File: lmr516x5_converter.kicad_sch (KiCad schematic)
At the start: 8 parts, among them U1 LMR516x5

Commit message: sch: first draft
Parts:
- added C1: 10uF 100V, Capacitor_SMD:C_1210_3225Metric, symbol Device:C_Small
- added C3: 0.1uF, Capacitor_SMD:C_0603_1608Metric, symbol Device:C_Small
- C1, C4: value 22uF 16V -> 10uF 50V
- R1: value 52.3k -> Vchoice; footprint Resistor_SMD:R_0603_1608Metric -> SMD:0603_1608Metric_DNI_NoPaste
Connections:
- net GND: now also C1.2, C3.2
- net Vin: now also C1.1, C3.1
- net 5V renamed Vout
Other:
- note added: "Just one of these entry capacitors seem be enough according to the datasheet."
- note added: "Vin max = 60V Vout max = 30V"
- moved on the sheet: C1, C2, C3, C4, L1, R1, R2, U1

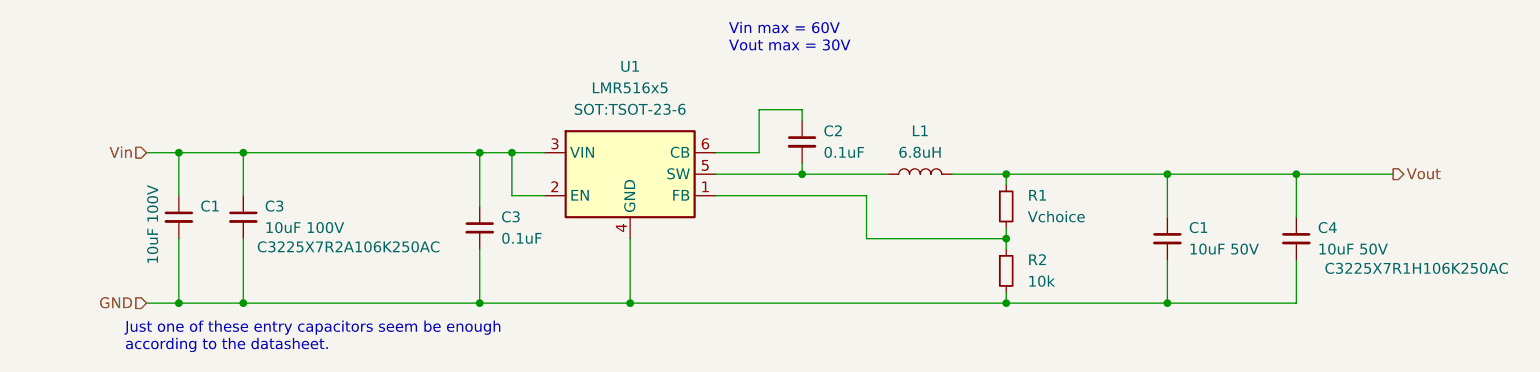
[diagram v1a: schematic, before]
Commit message: Change entry 0.1uF cap to 1uF 100V
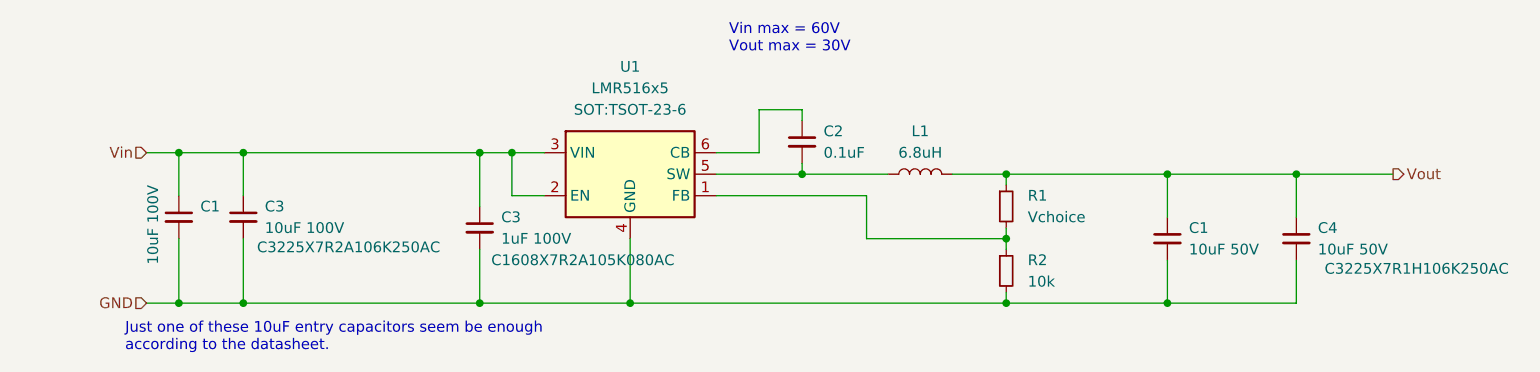
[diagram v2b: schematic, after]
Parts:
- C3: value 0.1uF -> 1uF 100V
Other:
- note added: "Just one of these 10uF entry capacitors seem be enough according to the datasheet."
- note removed: "Just one of these entry capacitors seem be enough according to the datasheet."
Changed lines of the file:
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@@
 		)
 	)
-	(text "Just one of these entry capacitors seem be enough\naccording to the datasheet."
+	(text "Just one of these 10uF entry capacitors seem be enough\naccording to the datasheet."
 		(exclude_from_sim no)
 		(at 36.83 53.594 0)
@@
 		(on_board yes)
 		(dnp no)
-		(fields_autoplaced yes)
 		(property "Reference" "C3"
 			(at 81.28 39.3762 0)
@@
 			)
 		)
-		(property "Value" "0.1uF"
+		(property "Value" "1uF 100V"
 			(at 81.28 41.9162 0)
 			(effects
@@
 			)
 		)
-		(property "Description" "Unpolarized capacitor, small symbol"
-			(at 78.74 40.64 0)
-			(effects
-				(font
-					(size 1.27 1.27)
-				)
-				(hide yes)
-			)
-		)
+		(property "Description" "C1608X7R2A105K080AC"
+			(at 90.932 44.45 0)
+			(effects
+				(font
+					(size 1.27 1.27)
+				)
+			)
+		)

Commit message: First placement
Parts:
- added C7: Csnub, Capacitor_SMD:C_0402_1005Metric, symbol Device:C_Small
- added R4: Rsnub, Resistor_SMD:R_0402_1005Metric, symbol Device:R_Small
- C1, C3: footprint Capacitor_SMD:C_1210_3225Metric -> SMD:C_1210_3225Metric_Tight
- C2, C3: footprint Capacitor_SMD:C_0603_1608Metric -> SMD:C_0603_1608Metric_Tight
- R1: footprint SMD:0603_1608Metric_DNI_NoPaste -> Resistor_SMD:R_0603_1608Metric
- U1: footprint SOT:TSOT-23-6 -> SOT:TSOT-23-6_Tight
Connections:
- net GND: now also R4.2
- net FB: now reaches R1.2, R2.1, U1.1 (FB)
- net at C2.2, L1.1, U1.5 (SW): now also C7.1
- new net: C7.2, R4.1
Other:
- note removed: "Just one of these 10uF entry capacitors seem be enough according to the datasheet."
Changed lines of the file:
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@@
 	(paper "A4")
 	(junction
+		(at 140.97 41.91)
+		(diameter 0)
+		(color 0 0 0 0)
+	)
+	(junction
+		(at 116.84 49.53)
+		(diameter 0)
+		(color 0 0 0 0)
+	)
+	(junction
 		(at 140.97 34.29)
 		(diameter 0)
@@
 	)
 	(junction
-		(at 140.97 41.91)
-		(diameter 0)
-		(color 0 0 0 0)
-	)
-	(junction
 		(at 116.84 34.29)
 		(diameter 0)
@@
 	(wire
 		(pts
+			(xy 116.84 34.29) (xy 116.84 36.83)
+		)
+		(stroke
+			(width 0)
+			(type default)
+		)
+	)
+	(wire
+		(pts
 			(xy 50.8 31.75) (xy 78.74 31.75)
 		)
@@
 	(wire
 		(pts
+			(xy 116.84 49.53) (xy 140.97 49.53)
+		)
+		(stroke
+			(width 0)
+			(type default)
+		)
+	)
+	(wire
+		(pts
 			(xy 50.8 49.53) (xy 78.74 49.53)
 		)
@@
 	(wire
 		(pts
-			(xy 96.52 49.53) (xy 140.97 49.53)
+			(xy 96.52 49.53) (xy 116.84 49.53)
 		)
 		(stroke
@@
 	(wire
 		(pts
+			(xy 140.97 41.91) (xy 140.97 43.18)
+		)
+		(stroke
+			(width 0)
+			(type default)
+		)
+	)
+	(wire
+		(pts
 			(xy 96.52 49.53) (xy 96.52 41.91)
 		)
@@
 	(wire
 		(pts
-			(xy 124.46 36.83) (xy 124.46 41.91)
-		)
-		(stroke
-			(width 0)
-			(type default)
-		)
-	)
-	(wire
-		(pts
-			(xy 124.46 41.91) (xy 140.97 41.91)
+			(xy 116.84 48.26) (xy 116.84 49.53)
 		)
 		(stroke
@@
 	(wire
 		(pts
+			(xy 106.68 36.83) (xy 110.49 36.83)
+		)
+		(stroke
+			(width 0)
+			(type default)
+		)
+	)
+	(wire
+		(pts
 			(xy 140.97 49.53) (xy 160.02 49.53)
 		)
@@
 	(wire
 		(pts
-			(xy 106.68 36.83) (xy 124.46 36.83)
-		)
-		(stroke
-			(width 0)
-			(type default)
-		)
-	)
-	(wire
-		(pts
 			(xy 78.74 31.75) (xy 82.55 31.75)
 		)
@@
 	(wire
 		(pts
-			(xy 140.97 41.91) (xy 140.97 43.18)
-		)
-		(stroke
-			(width 0)
-			(type default)
-		)
-	)
-	(wire
-		(pts
 			(xy 116.84 26.67) (xy 116.84 27.94)
 		)
@@
 	(wire
 		(pts
+			(xy 116.84 41.91) (xy 116.84 43.18)
+		)
+		(stroke
+			(width 0)
+			(type default)
+		)
+	)
+	(wire
+		(pts
 			(xy 140.97 34.29) (xy 140.97 35.56)
 		)
@@
 	(wire
 		(pts
+			(xy 140.97 41.91) (xy 137.16 41.91)
+		)
+		(stroke
+			(width 0)
+			(type default)
+		)
+	)
+	(wire
+		(pts
 			(xy 50.8 31.75) (xy 50.8 36.83)
 		)
@@
 			(width 0)
 			(type default)
-		)
-	)
-	(text "Just one of these 10uF entry capacitors seem be enough\naccording to the datasheet."
-		(exclude_from_sim no)
-		(at 36.83 53.594 0)
-		(effects
-			(font
-				(size 1.27 1.27)
-			)
-			(justify left)
 		)
 	)
@@
 			)
 			(justify left)
+		)
+	)
+	(label "FB"
+		(at 137.16 41.91 0)
+		(effects
+			(font
+				(size 1.27 1.27)
+			)
+			(justify left bottom)
+		)
+	)
+	(label "FB"
+		(at 110.49 36.83 180)
+		(effects
+			(font
+				(size 1.27 1.27)
+			)
+			(justify right bottom)
 		)
 	)
@@
 			)
 		)
-		(property "Footprint" "SOT:TSOT-23-6"
+		(property "Footprint" "SOT:TSOT-23-6_Tight"
 			(at 96.52 26.67 0)
 			(effects
@@
 			)
 		)
-		(property "Footprint" "Capacitor_SMD:C_1210_3225Metric"
+		(property "Footprint" "SMD:C_1210_3225Metric_Tight"
 			(at 43.18 39.37 0)
 			(effects
@@
 	)
 	(symbol
+		(lib_id "Device:R_Small")
+		(at 116.84 45.72 0)
+		(unit 1)
+		(exclude_from_sim no)
+		(in_bom yes)
+		(on_board yes)
+		(dnp no)
+		(fields_autoplaced yes)
+		(property "Reference" "R4"
+			(at 119.38 44.4499 0)
+			(effects
+				(font
+					(size 1.27 1.27)
+				)
+				(justify left)
+			)
+		)
+		(property "Value" "Rsnub"
+			(at 119.38 46.9899 0)
+			(effects
+				(font
+					(size 1.27 1.27)
+				)
+				(justify left)
+			)
+		)
+		(property "Footprint" "Resistor_SMD:R_0402_1005Metric"
+			(at 116.84 45.72 0)
+			(effects
+				(font
+					(size 1.27 1.27)
+				)
+				(hide yes)
+			)
+		)
+		(property "Datasheet" "~"
+			(at 116.84 45.72 0)
+			(effects
+				(font
+					(size 1.27 1.27)
+				)
+				(hide yes)
+			)
+		)
+		(property "Description" "Resistor, small symbol"
+			(at 116.84 45.72 0)
+			(effects
+				(font
+					(size 1.27 1.27)
+				)
+				(hide yes)
+			)
+		)
+		(pin "1"
+		)
+		(pin "2"
+		)
+		(instances
+			(project "project-hw-60v-dcdc"
+				(path "/bf513276-35b6-4c64-961b-f9ab0be6dcba/2aa74d1e-b615-4866-a6e6-81b2501e58da"
+					(reference "R4")
+					(unit 1)
+				)
+			)
+		)
+	)
+	(symbol
 		(lib_id "Device:C_Small")
 		(at 78.74 40.64 0)
@@
 			)
 		)
-		(property "Footprint" "Capacitor_SMD:C_0603_1608Metric"
+		(property "Footprint" "SMD:C_0603_1608Metric_Tight"
 			(at 78.74 40.64 0)
 			(effects
@@
 			)
 		)
-		(property "Footprint" "Capacitor_SMD:C_0603_1608Metric"
+		(property "Footprint" "SMD:C_0603_1608Metric_Tight"
 			(at 116.84 30.48 0)
 			(effects
@@
 			)
 		)
-		(property "Footprint" "Capacitor_SMD:C_1210_3225Metric"
+		(property "Footprint" "SMD:C_1210_3225Metric_Tight"
 			(at 50.8 39.37 0)
 			(effects
@@
 			)
 		)
-		(property "Footprint" "SMD:0603_1608Metric_DNI_NoPaste"
+		(property "Footprint" "Resistor_SMD:R_0603_1608Metric"
 			(at 140.97 38.1 0)
 			(effects
@@
 					(unit 1)
 				)
+			)
+		)
+	)
+	(symbol
+		(lib_id "Device:C_Small")
+		(at 116.84 39.37 0)
+		(unit 1)
+		(exclude_from_sim no)
+		(in_bom yes)
+		(on_board yes)
+		(dnp no)
+		(fields_autoplaced yes)
+		(property "Reference" "C7"
+			(at 119.38 38.1062 0)
+			(effects
+				(font
+					(size 1.27 1.27)
+				)
+				(justify left)
+			)
+		)
+		(property "Value" "Csnub"
+			(at 119.38 40.6462 0)
+			(effects
+				(font
+					(size 1.27 1.27)
+				)
+				(justify left)
+			)
+		)
+		(property "Footprint" "Capacitor_SMD:C_0402_1005Metric"
+			(at 116.84 39.37 0)
+			(effects
+				(font
+					(size 1.27 1.27)
+				)
+				(hide yes)
+			)
+		)
+		(property "Datasheet" "~"
+			(at 116.84 39.37 0)
+			(effects
+				(font
+					(size 1.27 1.27)
+				)
+				(hide yes)
+			)
+		)
+		(property "Description" "Unpolarized capacitor, small symbol"
+			(at 116.84 39.37 0)
+			(effects
+				(font
+					(size 1.27 1.27)
+				)
+				(hide yes)
+			)
+		)
+		(pin "2"
+		)
+		(pin "1"
+		)
+		(instances
+			(project "project-hw-60v-dcdc"
+				(path "/bf513276-35b6-4c64-961b-f9ab0be6dcba/2aa74d1e-b615-4866-a6e6-81b2501e58da"
+					(reference "C7")
+					(unit 1)
+				)

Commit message: First routing
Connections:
- net GND: now also C7.2; no longer R4.2
- net at C2.2, L1.1, U1.5 (SW): now also R4.1; no longer C7.1
- new net: C7.1, R4.2
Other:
- moved on the sheet: C7, R4
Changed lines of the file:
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@@
 	(symbol
 		(lib_id "Device:R_Small")
-		(at 116.84 45.72 0)
+		(at 116.84 39.37 0)
 		(unit 1)
 		(exclude_from_sim no)
@@
 		(fields_autoplaced yes)
 		(property "Reference" "R4"
-			(at 119.38 44.4499 0)
+			(at 119.38 38.0999 0)
 			(effects
 				(font
@@
 		)
 		(property "Value" "Rsnub"
-			(at 119.38 46.9899 0)
+			(at 119.38 40.6399 0)
 			(effects
 				(font
@@
 		)
 		(property "Footprint" "Resistor_SMD:R_0402_1005Metric"
-			(at 116.84 45.72 0)
-			(effects
-				(font
-					(size 1.27 1.27)
-				)
-				(hide yes)
-			)
-		)
-		(property "Datasheet" "~"
-			(at 116.84 45.72 0)
+			(at 116.84 39.37 0)
+			(effects
+				(font
+					(size 1.27 1.27)
+				)
+				(hide yes)
+			)
+		)
+		(property "Datasheet" "~"
+			(at 116.84 39.37 0)
 			(effects
 				(font
@@
 		)
 		(property "Description" "Resistor, small symbol"
-			(at 116.84 45.72 0)
+			(at 116.84 39.37 0)
 			(effects
 				(font
@@
 	(symbol
 		(lib_id "Device:C_Small")
-		(at 116.84 39.37 0)
+		(at 116.84 45.72 0)
 		(unit 1)
 		(exclude_from_sim no)
@@
 		(fields_autoplaced yes)
 		(property "Reference" "C7"
-			(at 119.38 38.1062 0)
+			(at 119.38 44.4562 0)
 			(effects
 				(font
@@
 		)
 		(property "Value" "Csnub"
-			(at 119.38 40.6462 0)
+			(at 119.38 46.9962 0)
 			(effects
 				(font
@@
 		)
 		(property "Footprint" "Capacitor_SMD:C_0402_1005Metric"
-			(at 116.84 39.37 0)
-			(effects
-				(font
-					(size 1.27 1.27)
-				)
-				(hide yes)
-			)
-		)
-		(property "Datasheet" "~"
-			(at 116.84 39.37 0)
+			(at 116.84 45.72 0)
+			(effects
+				(font
+					(size 1.27 1.27)
+				)
+				(hide yes)
+			)
+		)
+		(property "Datasheet" "~"
+			(at 116.84 45.72 0)
 			(effects
 				(font
@@
 		)
 		(property "Description" "Unpolarized capacitor, small symbol"
-			(at 116.84 39.37 0)
-			(effects
-				(font
+			(at 116.84 45.72 0)
+			(effects
+				(font
